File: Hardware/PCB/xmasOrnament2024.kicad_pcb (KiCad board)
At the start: 2 copper layers, 60 x 66.9 mm, 54 parts, among them IC1 TP4056-42, Q1 AO3401A, Q2 CJ3400, SW1 BZCN_TSA007A1518B03, SW2 BZCN_TSA007A1518B03, U1 STM32C011F6

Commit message: Fixes.
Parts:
- added R14: 100k, Borna KiCAD Library:R0603, F.Cu at (133.4, 107.0)
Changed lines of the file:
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@@
+		)
+	)
+	(footprint "Borna KiCAD Library:R0603"
+		(layer "F.Cu")
+		(at 133.425 107)
+		(descr "Resistor SMD 0603 (1608 Metric), square (rectangular) end terminal, IPC_7351 nominal, (Body size source: IPC-SM-782 page 72, https://www.pcb-3d.com/wordpress/wp-content/uploads/ipc-sm-782a_amendment_1_and_2.pdf), generated with kicad-footprint-generator")
+		(tags "resistor")
+		(property "Reference" "R14"
+			(at 0 -1.43 0)
+			(layer "User.1")
+			(effects
+				(font
+					(size 1 1)
+					(thickness 0.15)
+				)
+			)
+		)
+		(property "Value" "100k"
+			(at 0 1.43 0)
+			(layer "F.Fab")
+			(effects
+				(font
+					(size 1 1)
+					(thickness 0.15)
+				)
+			)
+		)
+		(property "Footprint" "Borna KiCAD Library:R0603"
+			(at 0 0 0)
+			(unlocked yes)
+			(layer "F.Fab")
+			(hide yes)
+			(effects
+				(font
+					(size 1.27 1.27)
+				)
+			)
+		)
+		(property "Datasheet" ""
+			(at 0 0 0)
+			(unlocked yes)
+			(layer "F.Fab")
+			(hide yes)
+			(effects
+				(font
+					(size 1.27 1.27)
+				)
+			)
+		)
+		(property "Description" ""
+			(at 0 0 0)
+			(unlocked yes)
+			(layer "F.Fab")
+			(hide yes)
+			(effects
+				(font
+					(size 1.27 1.27)
+				)
+			)
+		)
+		(sheetname "Root")
+		(sheetfile "xmasOrnamentV2.kicad_sch")
+		(attr smd)
+		(fp_line
+			(start -0.8 -0.4125)
+			(end 0.8 -0.4125)
+			(stroke
+				(width 0.1)
+				(type solid)
+			)
+			(layer "F.SilkS")
+		)
+		(fp_line
+			(start 0.8 0.4125)
+			(end -0.8 0.4125)
+			(stroke
+				(width 0.1)
+				(type solid)
+			)
+			(layer "F.SilkS")
+		)
+		(fp_line
+			(start -1.48 -0.73)
+			(end 1.48 -0.73)
+			(stroke
+				(width 0.05)
+				(type solid)
+			)
+			(layer "F.CrtYd")
+		)
+		(fp_line
+			(start -1.48 0.73)
+			(end -1.48 -0.73)
+			(stroke
+				(width 0.05)
+				(type solid)
+			)
+			(layer "F.CrtYd")
+		)
+		(fp_line
+			(start 1.48 -0.73)
+			(end 1.48 0.73)
+			(stroke
+				(width 0.05)
+				(type solid)
+			)
+			(layer "F.CrtYd")
+		)
+		(fp_line
+			(start 1.48 0.73)
+			(end -1.48 0.73)
+			(stroke
+				(width 0.05)
+				(type solid)
+			)
+			(layer "F.CrtYd")
+		)
+		(fp_line
+			(start -0.8 0.4125)
+			(end -0.8 -0.4125)
+			(stroke
+				(width 0.1)
+				(type solid)
+			)
+			(layer "F.Fab")
+		)
+		(fp_line
+			(start 0.8 -0.4125)
+			(end 0.8 0.4125)
+			(stroke
+				(width 0.1)
+				(type solid)
+			)
+			(layer "F.Fab")
+		)
+		(fp_text user "${REFERENCE}"
+			(at 0 2.5 0)
+			(layer "F.Fab")
+			(effects
+				(font
+					(size 0.4 0.4)
+					(thickness 0.06)
+				)
+			)
+		)
+		(pad "1" smd rect
+			(at -0.825 0)
+			(size 0.8 0.95)
+			(layers "F.Cu" "F.Paste" "F.Mask")
+			(net 38 "/SW_CLK")
+			(pintype "passive")
+		)
+		(pad "2" smd rect
+			(at 0.825 0)
+			(size 0.8 0.95)
+			(layers "F.Cu" "F.Paste" "F.Mask")
+			(net 1 "GND")
+			(pintype "passive")
+		)
+		(model "${KICAD6_3DMODEL_DIR}/Resistor_SMD.3dshapes/R_0603_1608Metric.wrl"
+			(offset
+				(xyz 0 0 0)
+			)
+			(scale
+				(xyz 1 1 1)
+			)
+			(rotate
+				(xyz 0 0 0)
+			)
 		)
 	)

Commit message: Board finished.
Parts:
- C4, R13: moved to F.Cu
- R14: moved to B.Cu
- moved R14 29.8 mm to (134.1, 77.2)
- moved TP5 20.9 mm to (130.4, 82.1)
- moved TP2 18.2 mm to (125.5, 82.1)
- moved TP1 17.7 mm to (128.1, 82.1)
- moved TP3 14.7 mm to (133.3, 82.1)
- moved TP4 14.0 mm to (136.2, 82.0)
- moved C3 13.3 mm to (132.3, 105.1), turned to 0 degrees
- moved R7 7.23 mm to (132.2, 112.7), turned to 90 degrees
- moved R6 6.30 mm to (130.6, 112.7), turned to 90 degrees
- moved Q1 5.23 mm to (128.0, 112.7), turned to -90 degrees
- moved R13 4.00 mm to (146.8, 98.5)
- moved C1 2.51 mm to (160.8, 117.0), turned to 135 degrees
- moved CONN1 2.15 mm to (161.4, 111.1)
- moved C4 1.88 mm to (140.8, 92.9), turned to -135 degrees
- moved R2 0.62 mm to (138.6, 114.0)
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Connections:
- C1 pad 2: Net-(IC1-BAT) -> VDD
- CONN1 pad +: Net-(IC1-BAT) -> VDD
- IC1 pad 5: Net-(IC1-BAT) -> VDD
- U1 pad 7: /BTN1 -> /BTN2
- U1 pad 9: /BTN2 -> /BTN1
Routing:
- net WS_SUPPLY: track 1.80 -> 215.0 mm, vias 0 -> 12
- net VDD: track 1.77 -> 165.6 mm, vias 0 -> 5
- net /WS_DIN: track 0.00 -> 50.4 mm, vias 0 -> 4
- net /PERIPH_SUPPLY: track 0.00 -> 41.1 mm, vias 0 -> 3
- net /RST: track 0.00 -> 26.3 mm, vias 0 -> 1
- net /BUZZER: track 0.00 -> 25.5 mm, vias 0 -> 1
- net /SW_CLK: track 0.00 -> 23.4 mm, vias 0 -> 1
- net /BTN2: track 7.62 -> 30.7 mm, vias 0 -> 1
- net Net-(IC1-CHRG): track 0.00 -> 18.9 mm, vias 0 -> 2
- net Net-(LED8-DO): track 0.00 -> 18.1 mm, vias 0 -> 2
- net Net-(LED7-DO): track 0.00 -> 18.1 mm, vias 0 -> 2
- net /SW_DIO: track 0.00 -> 16.6 mm, vias 0 -> 1
- net Net-(LED2-DO): track 0.00 -> 15.5 mm, vias 0 -> 2
- net Net-(LED4-DO): track 0.00 -> 15.1 mm, vias 0 -> 2
- net Net-(LED10-DO): track 0.00 -> 15.0 mm, vias 0 -> 2
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
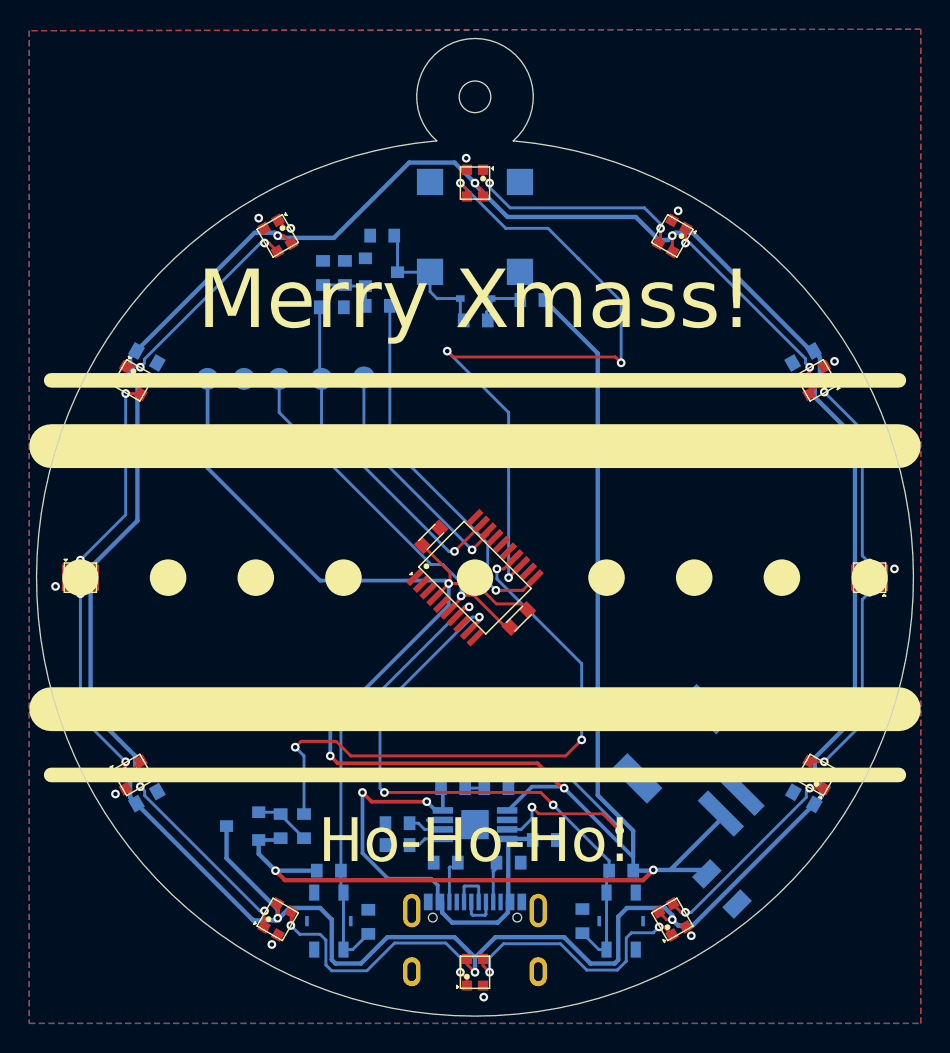
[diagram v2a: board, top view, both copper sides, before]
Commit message: Added VREG.
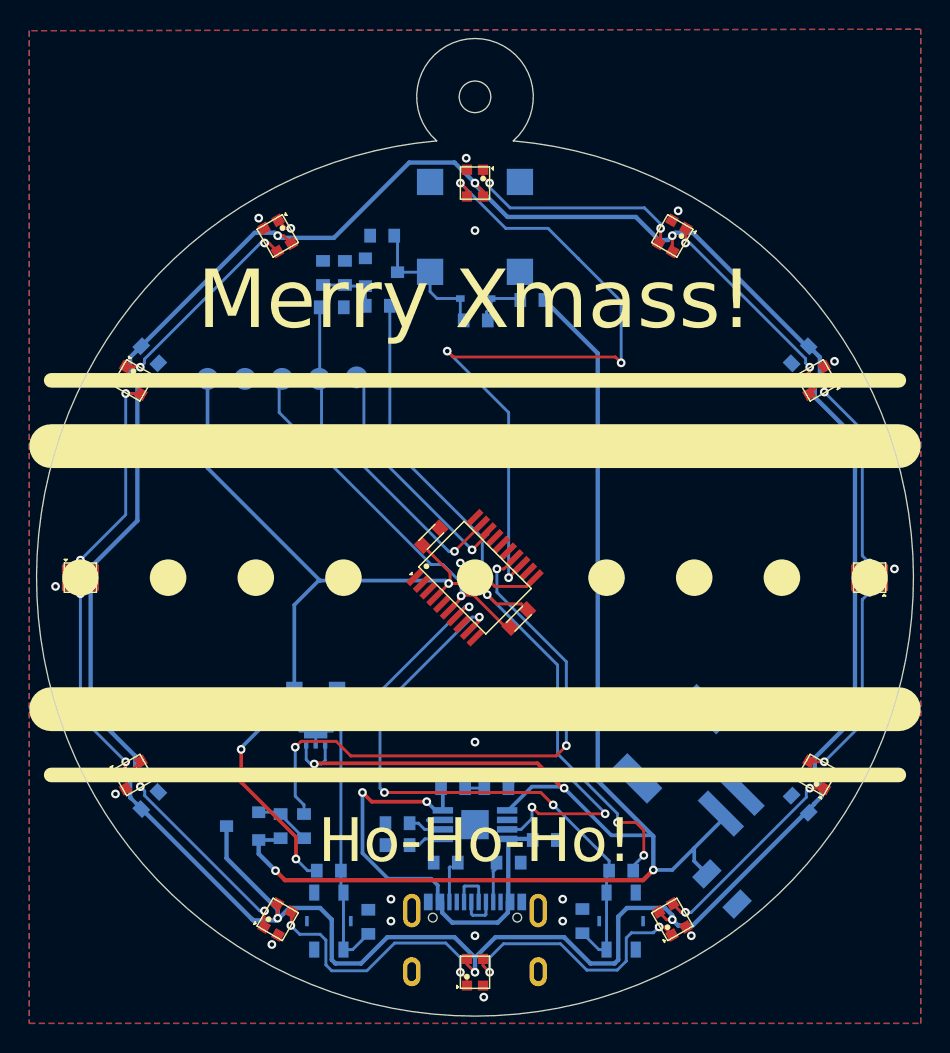
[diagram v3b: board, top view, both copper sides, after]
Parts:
- added U2: TPS7A2633DRVR, Borna KiCAD Library:WSON-6, B.Cu at (132.9, 106.2)
- moved C3 1.52 mm to (132.9, 103.7), turned to 180 degrees
- moved TP4 0.50 mm to (135.8, 82.0)
- moved C11 0.47 mm to (166.1, 111.2), turned to 135 degrees
- moved C5 0.28 mm to (121.6, 111.0), turned to 45 degrees
- moved C6 0.25 mm to (166.1, 80.5), turned to -135 degrees
- moved C12 0.25 mm to (121.6, 80.5), turned to 135 degrees
- moved TP5 0.20 mm to (130.7, 82.1)
- moved TP3 0.16 mm to (133.2, 82.1)
- moved TP1 0.06 mm to (128.1, 82.1)
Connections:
- C3 pad 2: VDD -> 3V3
- C4 pad 2: VDD -> 3V3
- R11 pad 1: VDD -> 3V3
- R12 pad 1: VDD -> 3V3
- R13 pad 2: VDD -> 3V3
- TP2 pad 1: VDD -> 3V3
- U1 pad 4: VDD -> 3V3
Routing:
- net 3V3: track 0.00 -> 87.6 mm, vias 0 -> 6
- net VDD: track 165.6 -> 114.8 mm, vias 5 -> 4
- net GND: track 1.03 -> 4.26 mm, vias 10 -> 18
- net Net-(IC1-CHRG): track 18.9 -> 15.9 mm
- net /PERIPH_SUPPLY: track 41.1 -> 39.8 mm
